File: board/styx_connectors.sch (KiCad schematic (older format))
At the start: 2 parts, among them J3 Conn_04x24, J4 Conn_04x24

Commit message: Board: initial schematic for the monitor interface board
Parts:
- removed J3, J4: Conn_04x24, agc_monitor:PinHeader_4x24_P2.54mm_Vertical, symbol agc_monitor:Conn_04x24
- added D10, D11, D4, D5, D6, D7, D8, D9: LED, symbol Device:LED
- added J3: Conn_01x06, symbol Connector_Generic:Conn_01x06
- added J4: Styx_P4, symbol agc_monitor:Styx_P4
- added J5: Styx_P5, symbol agc_monitor:Styx_P5
- added R21, R22, R23, R24, R25, R26, R27, R28: 330, symbol Device:R_US
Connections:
- net labels added: +3V3_FPGA, +3V3_IO, ADC_3V3_P, ADC_4SW_P, ADC_BPLSSW_P, DBG1, DBG2, DBG3, DBG4, DBLTST, DOSCAL, EN_3V3_AGC, GND, LED1, LED2, LED3, LED4, LED5, LED6, LED7, LED8, MAMU, MBR1, MBR2, MCTRAL_n, MDT01, MDT02, MDT03, MDT04, MDT05, MDT06, MDT07, MDT08, MDT09, MDT10, MDT11, MDT12, MDT13, MDT14, MDT15, MDT16, MGOJAM, MGP_n, MIIP, MINHL, MINKL, MLDCH, MLOAD, MNHNC, MNHRPT, MNHSBF, MNISQ, MON800, MONPAR, MONWBK, MONWT, MOSCAL_n, MPAL_n, MPIPAL_n, MRAG, MRCH, MRDCH, MREAD, MREQIN, MRGG, MRLG, MRPTAL_n, MRSC, MRULOG, MSBSTP, MSCAFL_n, MSCDBL_n, MSP, MSP803, MSP805, MSP806, MSP807, MSP902, MSP904, MSP908, MSP910, MSP912, MSP914, MSP916, MSQ10, MSQ11, MSQ12, MSQ13, MSQ14, MSQ16, MSQEXT, MST1, MST2, MST3, MSTP, MSTPIT_n, MSTRT, MT01, MT02, MT03, MT04, MT05, MT06, MT07, MT08, MT09, MT10, MT11, MT12, MTCAL_n, MTCSAI, MTCSA_n, MTLO, MVFAIL_n, MWAG, MWARNF_n, MWATCH_n, MWBBEG, MWBG, MWCH, MWEBG, MWFBG, MWG, MWL01, MWL02, MWL03, MWL04, MWL05, MWL06, MWL07, MWL08, MWL09, MWL10, MWL11, MWL12, MWL13, MWL14, MWL15, MWL16, MWLG, MWQG, MWSG, MWYG, MWZG, NHALGA_R, NHSTRT_R, OUTCOM, SIGNY_n
- wire segments 0 -> 260
- no-connect marks 0 -> 12
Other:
- note added: "ADC_3V3_N"
- note added: "ADC_4SW_N"
- note added: "ADC_BPLSSW_N"
- note added: "MTLO_N"

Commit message: Board: minor schematic tweaks, footprint creation, and initial subcircuit layout
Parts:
- removed D10, D11, D8, D9: LED, symbol Device:LED
- removed J3: Conn_01x06, symbol Connector_Generic:Conn_01x06
- removed R25, R26, R27, R28: 330, symbol Device:R_US
- added J3: Conn_01x10, Connector_PinHeader_2.54mm:PinHeader_2x05_P2.54mm_Vertical, symbol Connector_Generic:Conn_01x10
- D4, D5, D6, D7: footprint (none) -> LED_SMD:LED_0603_1608Metric
- J4, J5: footprint (none) -> agc_monitor:PinHeader_4x24_P2.54mm_Vertical
- R21, R22, R23, R24: footprint (none) -> Resistor_SMD:R_0603_1608Metric
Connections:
- net labels added: DBG5, DBG6, DBG7, DBG8
- net labels removed: LED5, LED6, LED7, LED8
- wire segments 260 -> 250
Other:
- moved on the sheet: D4, D5, D6, D7, R21, R22, R23, R24

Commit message: Board: minor redesign and initial ideas for layout
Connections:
- net NHSTRT2: now reaches J5.20 (N18)
- net NHALGA_R renamed NHALGA
- net NHSTRT_R renamed NHSTRT1
- no-connect marks 12 -> 11
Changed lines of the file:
@@
 	2650 5300 2700 5300
 Text GLabel 2650 6000 0    50   Output ~ 0
-NHALGA_R
+NHALGA
 Wire Wire Line
 	2650 6000 2700 6000
@@
 	3800 5300 3750 5300
 Text GLabel 3800 6000 2    50   Output ~ 0
-NHSTRT_R
+NHSTRT1
 Wire Wire Line
 	3800 6000 3750 6000
@@
 Wire Wire Line
 	7250 4200 7200 4200
-NoConn ~ 7200 4300
 Text GLabel 7250 4400 2    50   Output ~ 0
 MDT04
@@
 Wire Wire Line
 	3450 3500 3800 3500
+Text GLabel 7250 4300 2    50   Output ~ 0
+NHSTRT2
+Wire Wire Line
+	7250 4300 7200 4300
 $EndSCHEMATC

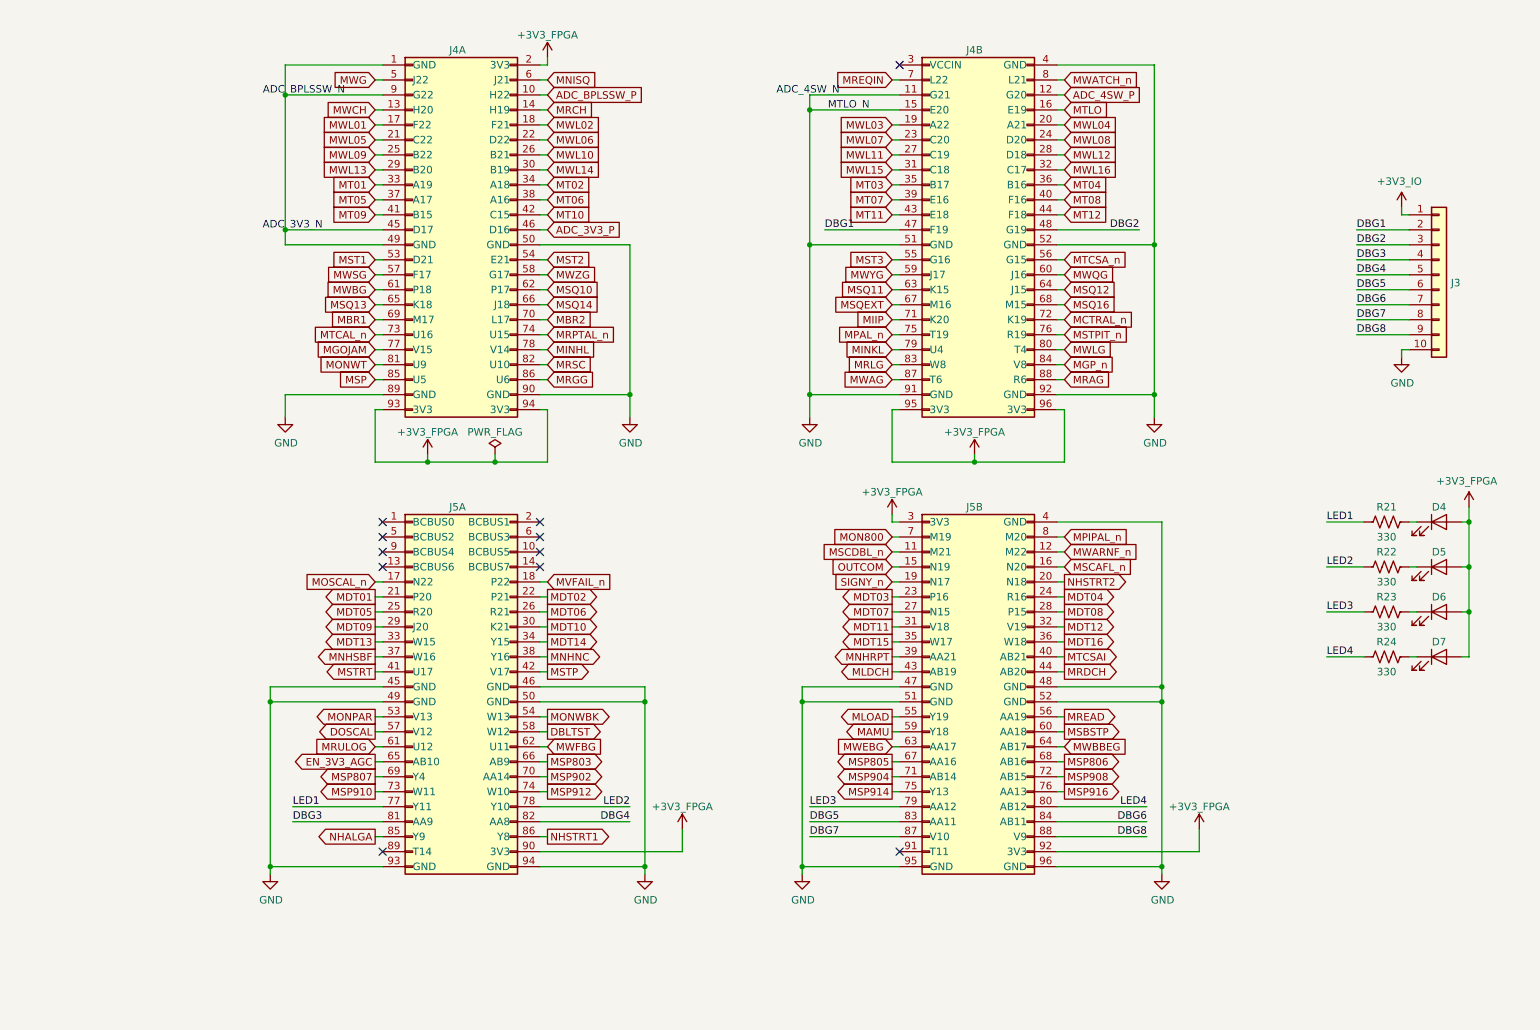
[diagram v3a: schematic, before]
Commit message: Board: lots of work routing connector J4. It's almost fully wired up; J5 is next.
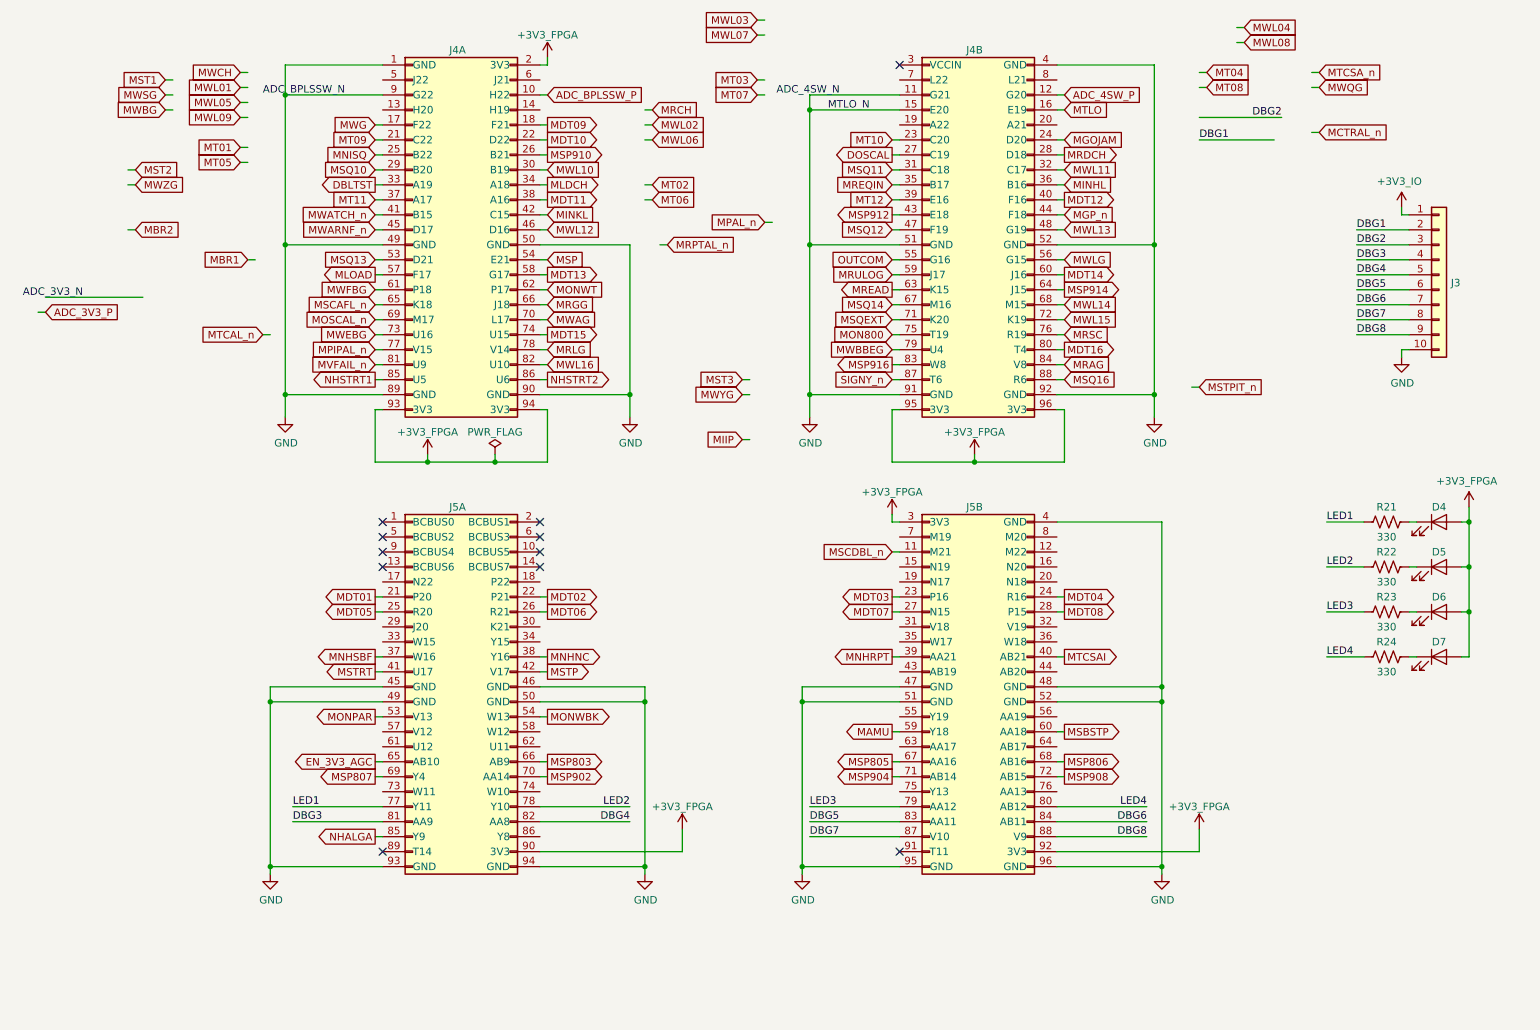
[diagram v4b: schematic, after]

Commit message: Board: completed routing of AGC signals to RNs and FPGA pins
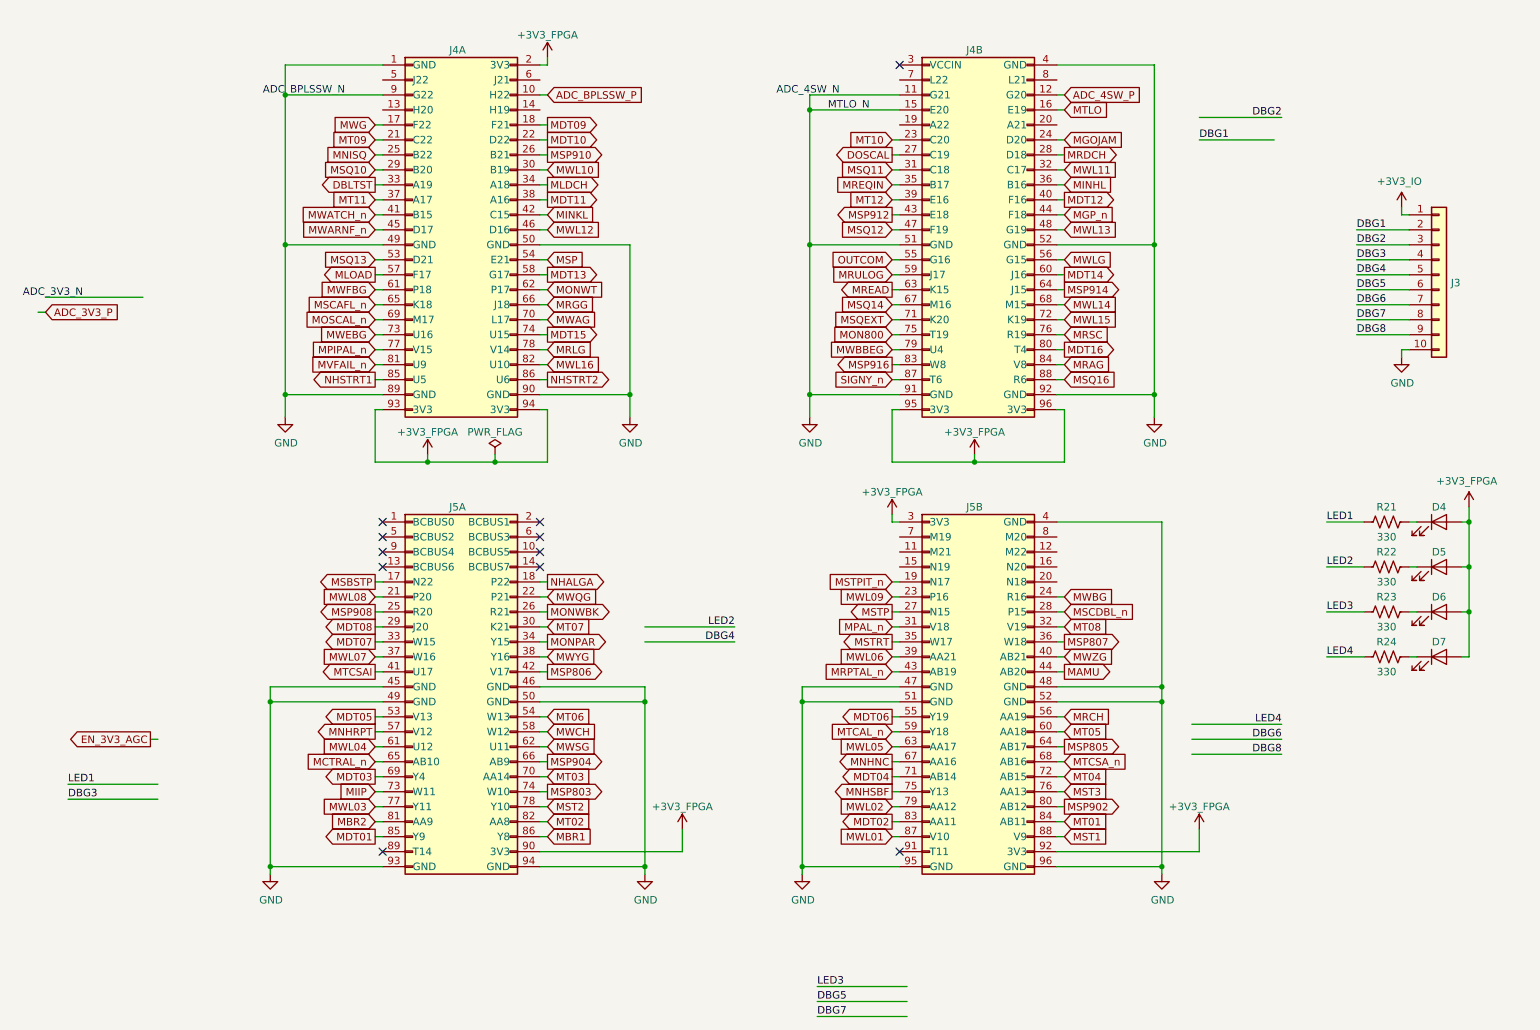
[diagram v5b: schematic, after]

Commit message: Board: Thinner traces for SI, more layout work, and some 3D models of parts
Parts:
- removed J3: Conn_01x10, Connector_PinHeader_2.54mm:PinHeader_2x05_P2.54mm_Vertical, symbol Connector_Generic:Conn_01x10
- added D8, D9: LED, LED_SMD:LED_0603_1608Metric, symbol Device:LED
- added J3: Conn_01x08, Connector_PinHeader_2.54mm:PinHeader_2x04_P2.54mm_Vertical, symbol Connector_Generic:Conn_01x08
- added R25, R26: 330, Resistor_SMD:R_0603_1608Metric, symbol Device:R_US
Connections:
- net labels added: LED5, LED6
- net labels removed: DBG7, DBG8
- wire segments 251 -> 260
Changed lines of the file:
@@
 	2700 1050 2050 1050
 Connection ~ 2050 1050
-Text Notes 1900 1050 0    50   ~ 0
+Text Notes 2100 1050 0    50   ~ 0
 ADC_BPLSSW_N
 Text GLabel 3800 5300 2    50   Input ~ 0
@@
 Wire Wire Line
 	7250 3150 7200 3150
-Text Notes 5750 1050 2    50   ~ 0
+Text Notes 6000 1050 2    50   ~ 0
 ADC_4SW_N
 Wire Wire Line
@@
 Connection ~ 5550 1150
 Wire Wire Line
-	5550 1150 5550 2050
+	5550 1150 5550 1250
 Text Notes 5950 1150 2    50   ~ 0
 MTLO_N
 Wire Wire Line
-	1100 2400 450  2400
-Text Notes 700  2400 2    50   ~ 0
+	6150 1250 5550 1250
+Text Notes 6000 1250 2    50   ~ 0
 ADC_3V3_N
-Text GLabel 450  2500 2    50   Input ~ 0
+Text GLabel 7250 1250 2    50   Input ~ 0
 ADC_3V3_P
 Wire Wire Line
-	450  2500 400  2500
+	7250 1250 7200 1250
 Text GLabel 2650 5800 0    50   Input ~ 0
 MWL03
@@
 Wire Wire Line
 	3800 4300 3750 4300
-Text GLabel 1150 5350 0    50   Output ~ 0
+Text GLabel 7250 4300 2    50   Output ~ 0
 EN_3V3_AGC
 Wire Wire Line
-	1200 5350 1150 5350
+	7200 4300 7250 4300
 Text GLabel 2650 2850 0    50   Input ~ 0
 MVFAIL_n
@@
 	6100 2850 6150 2850
 Wire Wire Line
-	1200 5650 600  5650
-Text Label 600  5650 0    50   ~ 0
+	2700 950  2450 950
+Text Label 2450 950  0    50   ~ 0
 LED1
 Wire Wire Line
-	4450 4600 5050 4600
-Text Label 5050 4600 2    50   ~ 0
+	3750 950  4000 950
+Text Label 4000 950  2    50   ~ 0
 LED2
 Wire Wire Line
-	6200 7000 5600 7000
-Text Label 5600 7000 0    50   ~ 0
+	6150 950  5900 950
+Text Label 5900 950  0    50   ~ 0
 LED3
 Wire Wire Line
-	8100 5250 8700 5250
-Text Label 8700 5250 2    50   ~ 0
+	7200 950  7450 950
+Text Label 7450 950  2    50   ~ 0
 LED4
 Wire Wire Line
-	1200 5750 600  5750
-Text Label 600  5750 0    50   ~ 0
-DBG3
-Wire Wire Line
-	4450 4700 5050 4700
-Text Label 5050 4700 2    50   ~ 0
-DBG4
-Wire Wire Line
-	6200 7100 5600 7100
-Text Label 5600 7100 0    50   ~ 0
-DBG5
-Wire Wire Line
-	8100 5350 8700 5350
-Text Label 8700 5350 2    50   ~ 0
-DBG6
-Wire Wire Line
-	8650 1350 8150 1350
-Text Label 8150 1350 0    50   ~ 0
+	6150 4000 5650 4000
+Text Label 5650 4200 0    50   ~ 0
 DBG1
 Wire Wire Line
-	8150 1200 8700 1200
-Text Label 8700 1200 2    50   ~ 0
+	7200 4000 7450 4000
+Text Label 7450 4200 2    50   ~ 0
 DBG2
-Wire Wire Line
-	6200 7200 5600 7200
-Text Label 5600 7200 0    50   ~ 0
-DBG7
-Wire Wire Line
-	8100 5450 8700 5450
-Text Label 8700 5450 2    50   ~ 0
-DBG8
 Wire Wire Line
 	7200 6100 8150 6100
@@
 L power:GND #PWR0157
 U 1 1 5E983484
-P 9500 2800
-F 0 "#PWR0157" H 9500 2550 50  0001 C CNN
-F 1 "GND" H 9505 2627 50  0000 C CNN
-F 2 "" H 9500 2800 50  0001 C CNN
-F 3 "" H 9500 2800 50  0001 C CNN
-	1    9500 2800
-	1    0    0    -1
-$EndComp
-Wire Wire Line
-	9500 2800 9500 2750
-Wire Wire Line
-	9500 2750 9550 2750
+P 9500 2600
+F 0 "#PWR0157" H 9500 2350 50  0001 C CNN
+F 1 "GND" H 9505 2427 50  0000 C CNN
+F 2 "" H 9500 2600 50  0001 C CNN
+F 3 "" H 9500 2600 50  0001 C CNN
+	1    9500 2600
+	1    0    0    -1
+$EndComp
+Wire Wire Line
+	9500 2600 9500 2550
+Wire Wire Line
+	9500 2550 9550 2550
 $Comp
 L agc_monitor:+3V3_IO #PWR0158
@@
 	9950 4800 9950 4500
 Connection ~ 9950 4500
-$Comp
-L Connector_Generic:Conn_01x10 J3
-U 1 1 5D1DF496
-P 9750 2250
-F 0 "J3" H 9829 2196 50  0000 L CNN
-F 1 "Conn_01x10" H 9830 2151 50  0001 L CNN
-F 2 "Connector_PinHeader_2.54mm:PinHeader_2x05_P2.54mm_Vertical" H 9750 2250 50  0001 C CNN
-F 3 "~" H 9750 2250 50  0001 C CNN
-	1    9750 2250
-	1    0    0    -1
-$EndComp
 Wire Wire Line
 	9550 2350 9200 2350
@@
 Text Label 9200 2450 0    50   ~ 0
 DBG6
-Wire Wire Line
-	9550 2550 9200 2550
-Text Label 9200 2550 0    50   ~ 0
-DBG7
-Wire Wire Line
-	9550 2650 9200 2650
-Text Label 9200 2650 0    50   ~ 0
-DBG8
 $Comp
 L power:PWR_FLAG #FLG0102
@@
 Connection ~ 2050 2050
 Connection ~ 2050 3050
+$Comp
+L Connector_Generic:Conn_01x08 J3
+U 1 1 5E56FA96
+P 9750 2150
+F 0 "J3" H 9830 2142 50  0000 L CNN
+F 1 "Conn_01x08" H 9830 2051 50  0000 L CNN
+F 2 "Connector_PinHeader_2.54mm:PinHeader_2x04_P2.54mm_Vertical" H 9750 2150 50  0001 C CNN
+F 3 "~" H 9750 2150 50  0001 C CNN
+	1    9750 2150
+	1    0    0    -1
+$EndComp
+$Comp
+L Device:LED D8
+U 1 1 5E5887E3
+P 9750 5100
+F 0 "D8" H 9750 5200 50  0000 C CNN
+F 1 "LED" H 9741 5225 50  0001 C CNN
+F 2 "LED_SMD:LED_0603_1608Metric" H 9750 5100 50  0001 C CNN
+F 3 "~" H 9750 5100 50  0001 C CNN
+	1    9750 5100
+	1    0    0    -1
+$EndComp
+Wire Wire Line
+	9250 5100 9000 5100
+Text Label 9000 5100 0    50   ~ 0
+LED5
+$Comp
+L Device:R_US R25
+U 1 1 5E5887EB
+P 9400 5100
+F 0 "R25" V 9300 5100 50  0000 C CNN
+F 1 "330" V 9500 5100 50  0000 C CNN
+F 2 "Resistor_SMD:R_0603_1608Metric" V 9440 5090 50  0001 C CNN
+F 3 "~" H 9400 5100 50  0001 C CNN
+	1    9400 5100
+	0    1    1    0
+$EndComp
+Wire Wire Line
+	9600 5100 9550 5100
+Wire Wire Line
+	9950 5100 9900 5100
+Wire Wire Line
+	9950 4800 9950 5100
+Connection ~ 9950 4800
+$Comp
+L Device:LED D9
+U 1 1 5E5B5AA7
+P 9750 5400
+F 0 "D9" H 9750 5500 50  0000 C CNN
+F 1 "LED" H 9741 5525 50  0001 C CNN
+F 2 "LED_SMD:LED_0603_1608Metric" H 9750 5400 50  0001 C CNN
+F 3 "~" H 9750 5400 50  0001 C CNN
+	1    9750 5400
+	1    0    0    -1
+$EndComp
+Wire Wire Line
+	9250 5400 9000 5400
+Text Label 9000 5400 0    50   ~ 0
+LED6
+$Comp
+L Device:R_US R26
+U 1 1 5E5B5AAF
+P 9400 5400
+F 0 "R26" V 9300 5400 50  0000 C CNN
+F 1 "330" V 9500 5400 50  0000 C CNN
+F 2 "Resistor_SMD:R_0603_1608Metric" V 9440 5390 50  0001 C CNN
+F 3 "~" H 9400 5400 50  0001 C CNN
+	1    9400 5400
+	0    1    1    0
+$EndComp
+Wire Wire Line
+	9600 5400 9550 5400
+Wire Wire Line
+	9950 5400 9900 5400
+Wire Wire Line
+	9950 5100 9950 5400
+Connection ~ 9950 5100
+Connection ~ 5550 1250
+Wire Wire Line
+	5550 1250 5550 2050
+Wire Wire Line
+	2700 1150 2450 1150
+Text Label 2450 1150 0    50   ~ 0
+LED5
+Wire Wire Line
+	3750 1150 4100 1150
+Wire Wire Line
+	4100 1150 4100 1200
+Wire Wire Line
+	4100 1200 4350 1200
+Text Label 4350 1200 2    50   ~ 0
+LED6
+Wire Wire Line
+	6150 4100 5650 4100
+Text Label 5650 4100 0    50   ~ 0
+DBG3
+Wire Wire Line
+	6150 4200 5650 4200
+Text Label 5650 4000 0    50   ~ 0
+DBG5
+Wire Wire Line
+	7200 4100 7450 4100
+Text Label 7450 4100 2    50   ~ 0
+DBG4
+Wire Wire Line
+	7200 4200 7450 4200
+Text Label 7450 4000 2    50   ~ 0
+DBG6
 $EndSCHEMATC
